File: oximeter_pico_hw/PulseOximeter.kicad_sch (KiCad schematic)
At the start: 25 parts, among them Q1 IRLML2060, Q2 IRLML2060, Q3 IRLML2060, Q4 IRLML2060, Q5 IRLML2060, Q6 IRLML2060, Q7 IRLML2060, U1 Pico, U2 SFH7060, U3 DC56-11YWA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

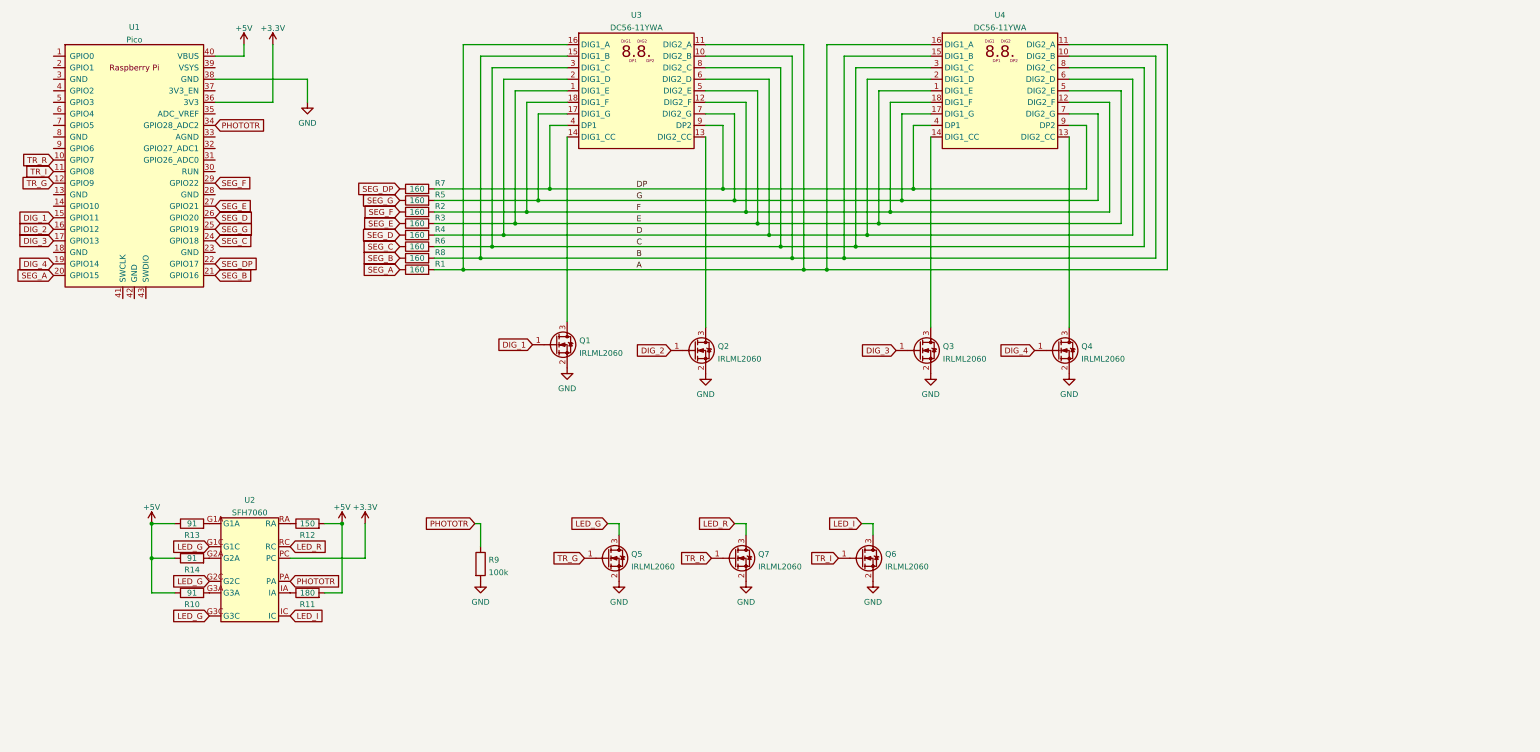
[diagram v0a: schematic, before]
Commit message: Update HW to revision 2
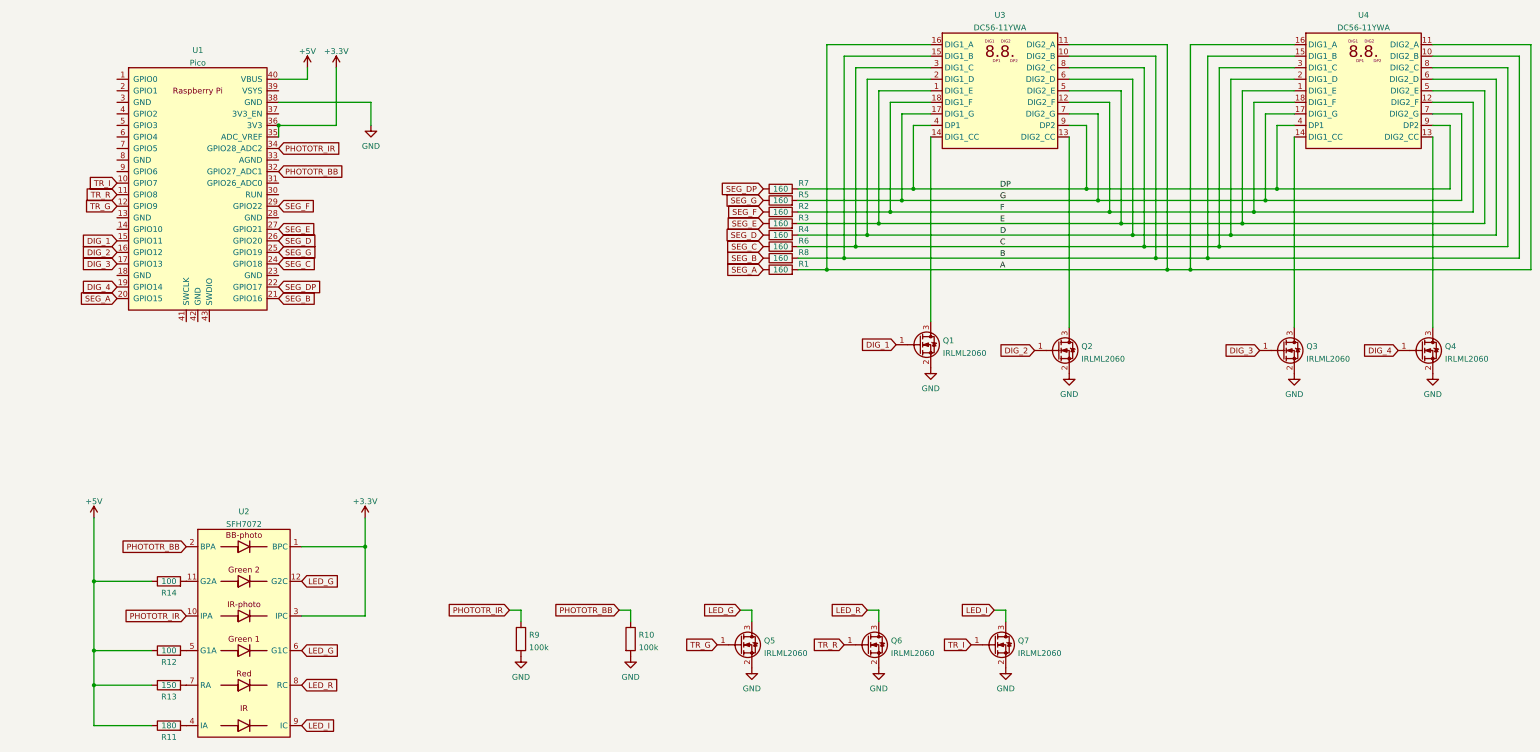
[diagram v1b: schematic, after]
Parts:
- removed U2: SFH7060, OptoDevice:SFH7060, symbol Sensor_Optical:SFH7060
- added U2: SFH7072, OptoDevice:SFH7072, symbol Sensor_Optical:SFH7072
- R1, R11, R2, R3, R4, R5, R6, R7, R8, R9: footprint Resistor_THT:R_Axial_DIN0204_L3.6mm_D1.6mm_P7.62mm_Horizontal -> Resistor_THT:R_Axial_DIN0207_L6.3mm_D2.5mm_P15.24mm_Horizontal
- R10: value 91 -> 100k; footprint Resistor_THT:R_Axial_DIN0204_L3.6mm_D1.6mm_P7.62mm_Horizontal -> Resistor_THT:R_Axial_DIN0207_L6.3mm_D2.5mm_P15.24mm_Horizontal
- R12: value 150 -> 100; footprint Resistor_THT:R_Axial_DIN0204_L3.6mm_D1.6mm_P7.62mm_Horizontal -> Resistor_THT:R_Axial_DIN0207_L6.3mm_D2.5mm_P15.24mm_Horizontal
- R13: value 91 -> 150; footprint Resistor_THT:R_Axial_DIN0204_L3.6mm_D1.6mm_P7.62mm_Horizontal -> Resistor_THT:R_Axial_DIN0207_L6.3mm_D2.5mm_P15.24mm_Horizontal
- R14: value 91 -> 100; footprint Resistor_THT:R_Axial_DIN0204_L3.6mm_D1.6mm_P7.62mm_Horizontal -> Resistor_THT:R_Axial_DIN0207_L6.3mm_D2.5mm_P15.24mm_Horizontal
- renumbered Q7 to Q6, Q6 to Q7
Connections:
- net +3V3: now also U1.35 (ADC_VREF), U2.1 (BPC), U2.3 (IPC)
- net +5V: now also R11.1, R12.1; no longer R10.1, R11.2, R12.2
- net GND: now also R10.2
- net LED_G: now also U2.12 (G2C), U2.6 (G1C)
- net LED_I: now also U2.9 (IC)
- net LED_R: now also U2.8 (RC)
- net TR_I: now also U1.10 (GPIO7); no longer U1.11 (GPIO8)
- net TR_R: now also U1.11 (GPIO8); no longer U1.10 (GPIO7)
- net PHOTOTR_BB: now reaches U1.32 (GPIO27_ADC1)
- net PHOTOTR_BB: now also R10.1, U2.2 (BPA)
- net at R14.2: now also U2.11 (G2A)
- net at R13.2: now also U2.7 (RA)
- net PHOTOTR renamed PHOTOTR_IR
- net PHOTOTR_IR: now also U2.10 (IPA)
- new net: R12.2, U2.5 (G1A)
- new net: R11.2, U2.4 (IA)
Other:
- company: (none) -> E-sektionens Teletekniska Avdelning
- title: (none) -> ETA's Pulse Oximeter
- moved on the sheet: Q1, Q2, Q3, Q4, Q5, Q6, Q7, R1, R2, R3, R4, R5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
